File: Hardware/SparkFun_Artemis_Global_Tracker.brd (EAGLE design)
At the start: 50.8 x 63.5 mm, 240 parts, among them J1 IRIDIUM_9603N, J2 USB-C, J6 U.FL, J7 ANTENNA-GROUNDEDEDGE_SMA, J8 STAND-OFF-REFLOW-M2.0_6.0MM_T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, J9 STAND-OFF-REFLOW-M2.0_6.0MM_T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, Q1 5.8A/30V/35mΩ, Q2 20V/4.2A/52mΩ/1.4W, Q3 20V/4.2A/52mΩ/1.4W, Q4 600mA/40V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

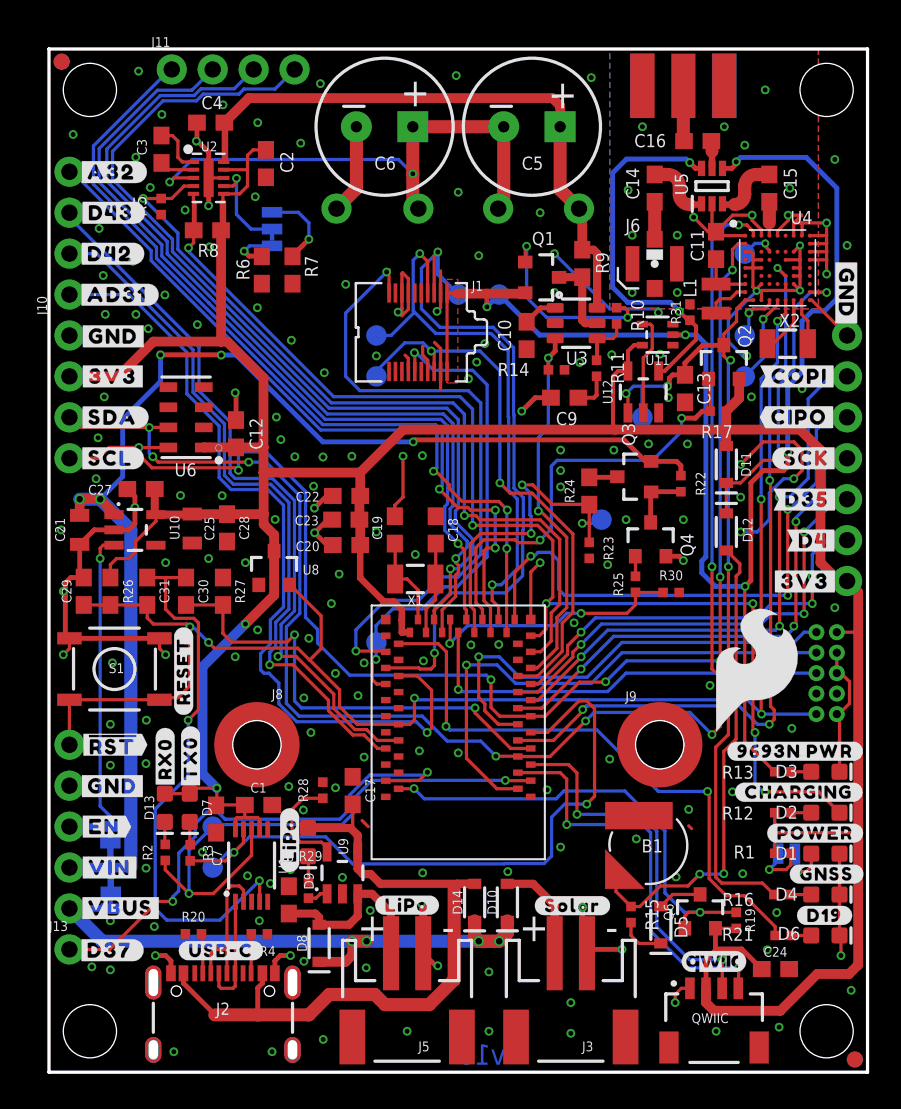
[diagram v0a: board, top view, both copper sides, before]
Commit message: design review changes
-measures cleaned up to avoid overlap
-LED labels to text only (and corrected 9603N typo)
-3.3V voltage regulator text in schematic (section label)
-corrected SPI SCK label on bottom
-D35 buzzard label turned to AD35 and round end
-D4 to round end label
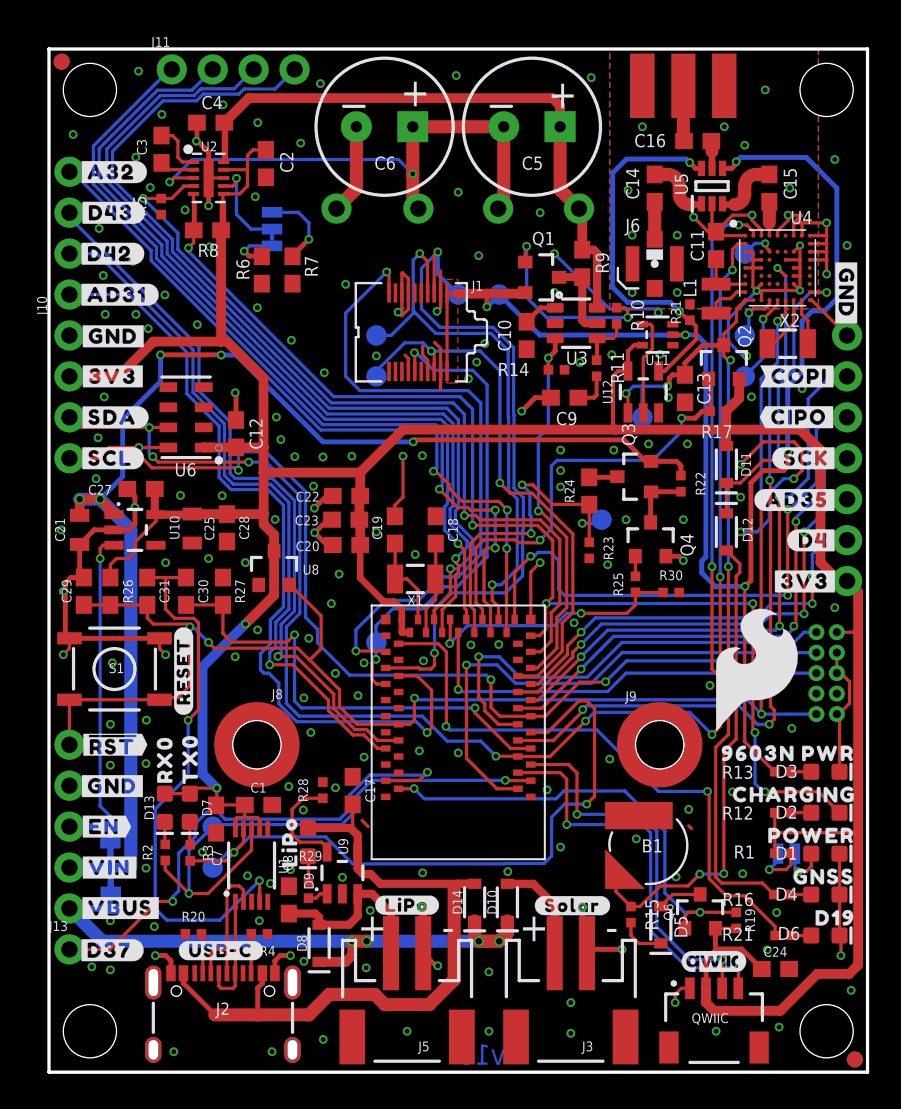
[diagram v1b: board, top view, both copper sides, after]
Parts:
- removed U$23: (no value), output:#TX0#163
- removed U$49: (no value), output:#RX0#163
- removed U$62: (no value), output:#D35#0
- removed U$68: (no value), output:#D4#9697
- added U$93: (no value), output:9603N_PWR40
- added U$94: (no value), output:POWER9605
- added U$95: (no value), output:GNSS9606
- added U$96: (no value), output:D199607
- U$12: device output:#D4#0 -> output:LIPO5
- U$16: device output:#LIPO#163 -> output:RX06
- U$18: device output:#D35#9697 -> output:TX07
- U$19: device output:#POWER#21 -> output:#AD35#199609
- U$2: device output:#CHARGING#22 -> output:#SCK#199608
- U$29: device output:#D19#0 -> output:#AD35#0
- U$50: device output:#GNSS#20 -> output:#D4#36
- U$63: device output:#SCL#1 -> output:#D4#5
- U$9: device output:#9693N_PWR#23 -> output:CHARGING9604
- moved U$18 41.5 mm to (8.77, 19.4), turned to 90 degrees
- moved U$12 37.4 mm to (14.9, 14.3), flipped to the top, turned to 90 degrees
- moved U$29 25.8 mm to (46.4, 35.5), flipped to the bottom
- moved U$2 20.7 mm to (47.0, 38.1), flipped to the bottom
- moved U$19 20.7 mm to (46.4, 35.5)
- moved U$50 20.7 mm to (47.4, 33.0), flipped to the bottom
- moved U$16 9.21 mm to (7.20, 19.4)
- moved U$63 5.07 mm to (47.5, 33.0), flipped to the top
- moved U$9 2.70 mm to (46.3, 17.2)

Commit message: eng checklist run
nudged some vias to avoid hitting silk labels
-fixed some PROD_IDs
-a little SCH cleaning
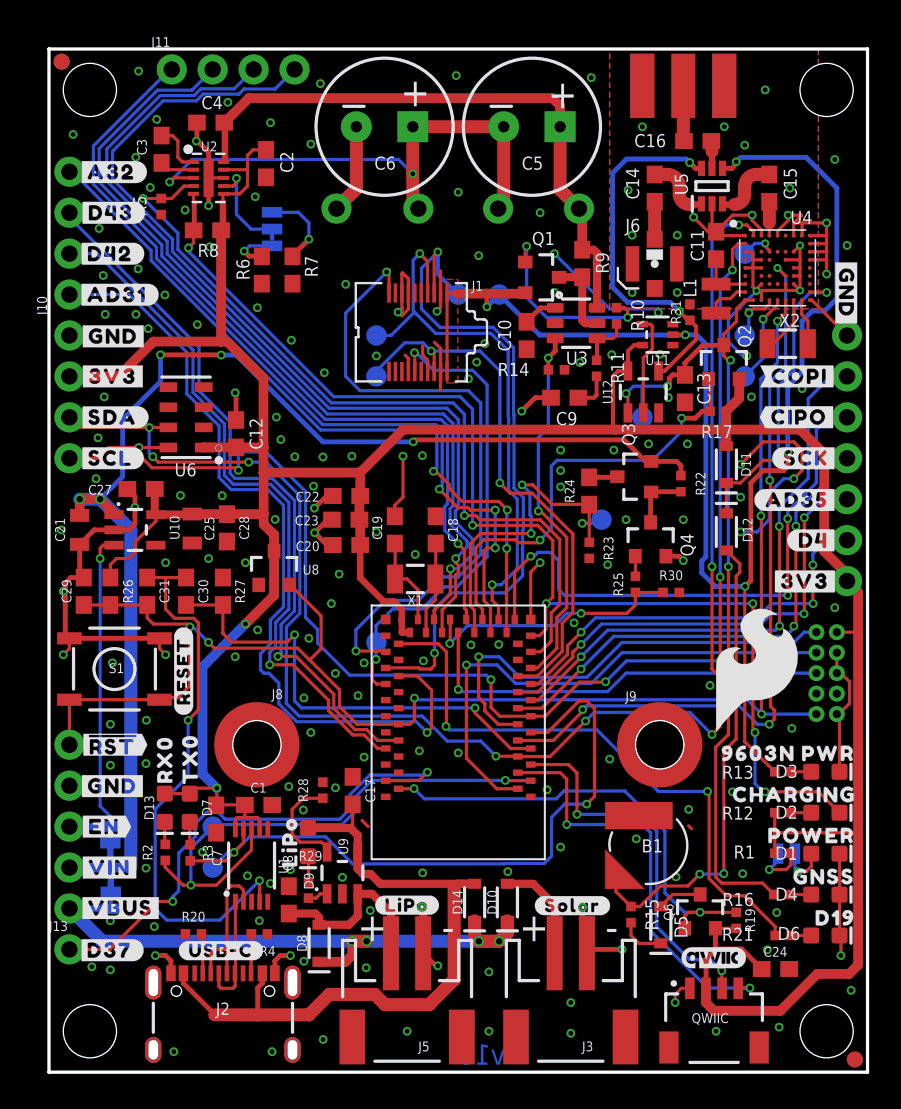
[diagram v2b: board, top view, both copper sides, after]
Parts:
- moved U$11 0.23 mm to (41.3, 7.09)
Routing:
- net ARTEMIS_RX0: track 35.2 -> 34.1 mm
- net ARTEMIS_D39_SCL4: track 25.2 -> 25.9 mm
- net ARTEMIS_D35: track 28.5 -> 29.0 mm

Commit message: R9 Current Sense Resistor Value changed to 15mOhm
Switched in-rush current sense resistor from 12mOhms to 15mOhms. This value is easier to source. It changes the in-rush current sense from 4.2A to 3.3A.

Also added datasheet for in-rush current protection IC: ADM4210
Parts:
- R9: value 0.012ohm -> 0.015ohm
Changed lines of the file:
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@@
 <drawing>
 <settings>
-<setting alwaysvectorfont="yes"/>
+<setting alwaysvectorfont="no"/>
 <setting keepoldvectorfont="yes"/>
 <setting verticaltext="up"/>
 </settings>
-<grid distance="0.05" unitdist="inch" unit="inch" style="lines" multiple="1" display="yes" altdistance="0.0001" altunitdist="inch" altunit="inch"/>
+<grid distance="0.05" unitdist="inch" unit="inch" style="lines" multiple="1" display="yes" altdistance="0.005" altunitdist="inch" altunit="inch"/>
 <layers>
 <layer number="1" name="Top" color="4" fill="1" visible="yes" active="yes"/>
@@
 <layer number="47" name="Measures" color="7" fill="1" visible="no" active="yes"/>
 <layer number="48" name="Document" color="7" fill="1" visible="no" active="yes"/>
-<layer number="49" name="Reference" color="7" fill="1" visible="yes" active="yes"/>
+<layer number="49" name="Reference" color="7" fill="1" visible="no" active="yes"/>
 <layer number="50" name="dxf" color="7" fill="1" visible="no" active="yes"/>
 <layer number="51" name="tDocu" color="6" fill="1" visible="yes" active="yes"/>
@@
 <attribute name="PROD_ID" value="RES-14962" x="35.2298" y="46.9392" size="1.778" layer="27" rot="R270" display="off"/>
 </element>
-<element name="R9" library="SparkFun-Resistors" package="0603" value="0.012ohm" x="33.0962" y="50.1904" smashed="yes" rot="R90">
+<element name="R9" library="SparkFun-Resistors" package="0603" value="0.015ohm" x="33.0962" y="50.1904" smashed="yes" rot="R90">
 <attribute name="NAME" x="34.7472" y="49.5554" size="0.8128" layer="25" font="vector" ratio="18" rot="R90"/>
-<attribute name="PROD_ID" value="RES-14691" x="33.0962" y="50.1904" size="1.778" layer="27" rot="R90" display="off"/>
-<attribute name="VALUE" value="0.012ohm" x="33.8582" y="51.9684" size="0.4064" layer="27" font="vector" ratio="10" rot="R90"/>
+<attribute name="PROD_ID" value="RES-16305" x="33.0962" y="50.1904" size="1.778" layer="27" rot="R90" display="off"/>
+<attribute name="VALUE" value="0.015ohm" x="33.8582" y="51.9684" size="0.4064" layer="27" font="vector" ratio="10" rot="R90"/>
 </element>
 <element name="R11" library="SparkFun-Resistors" package="0402-TIGHT" value="100" x="33.9852" y="43.688" smashed="yes" rot="R270">

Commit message: AND Gate (U12) PROD_ID update to correct package
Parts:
- U12: value 74LVC1G08SE -> 74LVC1G08W5-7
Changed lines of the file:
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@@
 <attribute name="PROD_ID" value="HW-14879" x="37.9032" y="20.32" size="1.778" layer="27" display="off"/>
 </element>
-<element name="U12" library="SparkFun-IC-Logic" package="SOT23-5" value="74LVC1G08SE" x="36.8808" y="42.2148" smashed="yes">
+<element name="U12" library="SparkFun-IC-Logic" package="SOT23-5" value="74LVC1G08W5-7" x="36.8808" y="42.2148" smashed="yes">
 <attribute name="NAME" x="34.9758" y="42.2148" size="0.6096" layer="25" font="vector" ratio="20" rot="R90" align="bottom-center"/>
-<attribute name="PROD_ID" value="IC-10841" x="36.8808" y="42.2148" size="1.778" layer="27" font="vector" ratio="15" display="off"/>
-<attribute name="VALUE" x="39.4208" y="42.2148" size="0.6096" layer="27" font="vector" ratio="20" rot="R90" align="bottom-center"/>
+<attribute name="PROD_ID" value="IC-16359" x="36.8808" y="42.2148" size="1.778" layer="27" font="vector" ratio="15" display="off"/>
+<attribute name="VALUE" value="74LVC1G08W5-7" x="39.4208" y="42.2148" size="0.6096" layer="27" font="vector" ratio="20" rot="R90" align="bottom-center"/>
 </element>
 <element name="U11" library="SparkFun-IC-Logic" package="SOT353" value="74LVC1G04SE" x="37.7698" y="45.7708" smashed="yes" rot="R90">
